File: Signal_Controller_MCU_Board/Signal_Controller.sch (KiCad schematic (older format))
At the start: 50 parts, among them J1 BARREL_JACK, J2 USB_OTG, J3 CONN_02X03, J4 CONN_01X03, J5 CONN_01X02, J6 CONN_01X02, J7 CONN_01X02, J8 CONN_01X07, Q1 2N7002P,215, Q2 2N7002P,215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

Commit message: Both boards mostly completed
just need final tweaks, silkscreen stuff etc, all major routing and
placement done
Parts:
- removed J7: CONN_01X02, symbol CONN_01X02
- added C10: CP1, Capacitors_THT:CP_Radial_D6.3mm_P2.50mm, symbol CP1
- C7, C8: value 18pF -> 22pF
- Y1: footprint (none) -> Crystals:Crystal_SMD_3225-4pin_3.2x2.5mm
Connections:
- net +12V: now also C10.1
- net COIL_1A: now also J5.1 (P1); no longer J5.2 (P2)
- net COIL_1B: now also J5.2 (P2); no longer J5.1 (P1)
- net GND: now also C10.2
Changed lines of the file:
@@
 $EndComp
 $Comp
-L GND #PWR01
+L GND #PWR19
 U 1 1 58F58032
 P 4600 5850
-F 0 "#PWR01" H 4600 5600 50  0001 C CNN
+F 0 "#PWR19" H 4600 5600 50  0001 C CNN
 F 1 "GND" H 4600 5700 50  0000 C CNN
 F 2 "" H 4600 5850 50  0001 C CNN
@@
 $EndComp
 $Comp
-L GND #PWR02
+L GND #PWR1
 U 1 1 58F581C2
 P 950 3550
-F 0 "#PWR02" H 950 3300 50  0001 C CNN
+F 0 "#PWR1" H 950 3300 50  0001 C CNN
 F 1 "GND" H 950 3400 50  0000 C CNN
 F 2 "" H 950 3550 50  0001 C CNN
@@
 $EndComp
 $Comp
-L GND #PWR03
+L GND #PWR9
 U 1 1 58F6B32F
 P 3250 1750
-F 0 "#PWR03" H 3250 1500 50  0001 C CNN
+F 0 "#PWR9" H 3250 1500 50  0001 C CNN
 F 1 "GND" H 3250 1600 50  0000 C CNN
 F 2 "" H 3250 1750 50  0001 C CNN
@@
 $EndComp
 $Comp
-L +5V #PWR04
+L +5V #PWR17
 U 1 1 58F6B398
 P 4300 1050
-F 0 "#PWR04" H 4300 900 50  0001 C CNN
+F 0 "#PWR17" H 4300 900 50  0001 C CNN
 F 1 "+5V" H 4300 1190 50  0000 C CNN
 F 2 "" H 4300 1050 50  0001 C CNN
@@
 $EndComp
 $Comp
-L +12V #PWR05
+L +12V #PWR8
 U 1 1 58F6B3C8
 P 2550 1050
-F 0 "#PWR05" H 2550 900 50  0001 C CNN
+F 0 "#PWR8" H 2550 900 50  0001 C CNN
 F 1 "+12V" H 2550 1190 50  0000 C CNN
 F 2 "" H 2550 1050 50  0001 C CNN
@@
 $EndComp
 $Comp
-L GND #PWR06
+L GND #PWR16
 U 1 1 58F6B932
 P 4150 2100
-F 0 "#PWR06" H 4150 1850 50  0001 C CNN
+F 0 "#PWR16" H 4150 1850 50  0001 C CNN
 F 1 "GND" H 4150 1950 50  0000 C CNN
 F 2 "" H 4150 2100 50  0001 C CNN
@@
 $EndComp
 $Comp
-L +12V #PWR07
+L +12V #PWR4
 U 1 1 58F6BF50
 P 1350 1050
-F 0 "#PWR07" H 1350 900 50  0001 C CNN
+F 0 "#PWR4" H 1350 900 50  0001 C CNN
 F 1 "+12V" H 1350 1190 50  0000 C CNN
 F 2 "" H 1350 1050 50  0001 C CNN
@@
 $EndComp
 $Comp
-L GND #PWR08
+L GND #PWR5
 U 1 1 58F6BFB3
-P 1350 1450
-F 0 "#PWR08" H 1350 1200 50  0001 C CNN
-F 1 "GND" H 1350 1300 50  0000 C CNN
-F 2 "" H 1350 1450 50  0001 C CNN
-F 3 "" H 1350 1450 50  0001 C CNN
-	1    1350 1450
+P 1350 1600
+F 0 "#PWR5" H 1350 1350 50  0001 C CNN
+F 1 "GND" H 1350 1450 50  0000 C CNN
+F 2 "" H 1350 1600 50  0001 C CNN
+F 3 "" H 1350 1600 50  0001 C CNN
+	1    1350 1600
 	1    0    0    -1
 $EndComp
@@
 $EndComp
 $Comp
-L +5V #PWR09
+L +5V #PWR12
 U 1 1 58F6C802
 P 3300 3800
-F 0 "#PWR09" H 3300 3650 50  0001 C CNN
+F 0 "#PWR12" H 3300 3650 50  0001 C CNN
 F 1 "+5V" H 3300 3940 50  0000 C CNN
 F 2 "" H 3300 3800 50  0001 C CNN
@@
 $EndComp
 $Comp
-L GND #PWR010
+L GND #PWR13
 U 1 1 58F6D034
 P 3300 4800
-F 0 "#PWR010" H 3300 4550 50  0001 C CNN
+F 0 "#PWR13" H 3300 4550 50  0001 C CNN
 F 1 "GND" H 3300 4650 50  0000 C CNN
 F 2 "" H 3300 4800 50  0001 C CNN
@@
 $EndComp
 $Comp
-L +5V #PWR011
+L +5V #PWR18
 U 1 1 58F6D787
 P 4600 2750
-F 0 "#PWR011" H 4600 2600 50  0001 C CNN
+F 0 "#PWR18" H 4600 2600 50  0001 C CNN
 F 1 "+5V" H 4600 2890 50  0000 C CNN
 F 2 "" H 4600 2750 50  0001 C CNN
@@
 MOSI
 $Comp
-L +5V #PWR012
+L +5V #PWR21
 U 1 1 58F6E151
 P 6000 1150
-F 0 "#PWR012" H 6000 1000 50  0001 C CNN
+F 0 "#PWR21" H 6000 1000 50  0001 C CNN
 F 1 "+5V" H 6000 1290 50  0000 C CNN
 F 2 "" H 6000 1150 50  0001 C CNN
@@
 $EndComp
 $Comp
-L GND #PWR013
+L GND #PWR22
 U 1 1 58F6E17B
 P 6000 1550
-F 0 "#PWR013" H 6000 1300 50  0001 C CNN
+F 0 "#PWR22" H 6000 1300 50  0001 C CNN
 F 1 "GND" H 6000 1400 50  0000 C CNN
 F 2 "" H 6000 1550 50  0001 C CNN
@@
 $EndComp
 $Comp
-L GND #PWR014
+L GND #PWR7
 U 1 1 58F6F39D
 P 1950 3650
-F 0 "#PWR014" H 1950 3400 50  0001 C CNN
+F 0 "#PWR7" H 1950 3400 50  0001 C CNN
 F 1 "GND" H 1950 3500 50  0000 C CNN
 F 2 "" H 1950 3650 50  0001 C CNN
@@
 F 0 "Y1" H 4100 5050 50  0000 C CNN
 F 1 "Crystal" V 3950 5050 50  0000 C CNN
-F 2 "" H 4100 4900 50  0001 C CNN
+F 2 "Crystals:Crystal_SMD_3225-4pin_3.2x2.5mm" H 4100 4900 50  0001 C CNN
 F 3 "" H 4100 4900 50  0001 C CNN
 	1    4100 4900
@@
 P 3850 4700
 F 0 "C7" V 3800 4550 50  0000 L CNN
-F 1 "18pF" V 3900 4450 50  0000 L CNN
+F 1 "22pF" V 3900 4450 50  0000 L CNN
 F 2 "Capacitors_SMD:C_0603" H 3888 4550 50  0001 C CNN
 F 3 "" H 3850 4700 50  0001 C CNN
@@
 P 3850 5100
 F 0 "C8" V 3900 4950 50  0000 L CNN
-F 1 "18pF" V 3800 4850 50  0000 L CNN
+F 1 "22pF" V 3800 4850 50  0000 L CNN
 F 2 "Capacitors_SMD:C_0603" H 3888 4950 50  0001 C CNN
 F 3 "" H 3850 5100 50  0001 C CNN
@@
 $EndComp
 $Comp
-L GND #PWR015
+L GND #PWR14
 U 1 1 58F6FF32
 P 3650 5300
-F 0 "#PWR015" H 3650 5050 50  0001 C CNN
+F 0 "#PWR14" H 3650 5050 50  0001 C CNN
 F 1 "GND" H 3650 5150 50  0000 C CNN
 F 2 "" H 3650 5300 50  0001 C CNN
@@
 $EndComp
 $Comp
-L GND #PWR016
+L GND #PWR25
 U 1 1 58F716B0
 P 8000 5850
-F 0 "#PWR016" H 8000 5600 50  0001 C CNN
+F 0 "#PWR25" H 8000 5600 50  0001 C CNN
 F 1 "GND" H 8000 5700 50  0000 C CNN
 F 2 "" H 8000 5850 50  0001 C CNN
@@
 $EndComp
 $Comp
-L GND #PWR017
+L GND #PWR15
 U 1 1 58F71A74
 P 3900 3350
-F 0 "#PWR017" H 3900 3100 50  0001 C CNN
+F 0 "#PWR15" H 3900 3100 50  0001 C CNN
 F 1 "GND" H 3900 3200 50  0000 C CNN
 F 2 "" H 3900 3350 50  0001 C CNN
@@
 $EndComp
 $Comp
-L +5V #PWR018
+L +5V #PWR10
 U 1 1 58F73DF5
 P 3300 2750
-F 0 "#PWR018" H 3300 2600 50  0001 C CNN
+F 0 "#PWR10" H 3300 2600 50  0001 C CNN
 F 1 "+5V" H 3300 2890 50  0000 C CNN
 F 2 "" H 3300 2750 50  0001 C CNN
@@
 $EndComp
 $Comp
-L GND #PWR019
+L GND #PWR11
 U 1 1 58F73E45
 P 3300 3350
-F 0 "#PWR019" H 3300 3100 50  0001 C CNN
+F 0 "#PWR11" H 3300 3100 50  0001 C CNN
 F 1 "GND" H 3300 3200 50  0000 C CNN
 F 2 "" H 3300 3350 50  0001 C CNN
@@
 $EndComp
 $Comp
-L +12V #PWR020
+L +12V #PWR26
 U 1 1 58F75C3C
 P 9050 1100
-F 0 "#PWR020" H 9050 950 50  0001 C CNN
+F 0 "#PWR26" H 9050 950 50  0001 C CNN
 F 1 "+12V" H 9050 1240 50  0000 C CNN
 F 2 "" H 9050 1100 50  0001 C CNN
@@
 $EndComp
 $Comp
-L +12V #PWR021
+L +12V #PWR27
 U 1 1 58F76B58
 P 9050 3050
-F 0 "#PWR021" H 9050 2900 50  0001 C CNN
+F 0 "#PWR27" H 9050 2900 50  0001 C CNN
 F 1 "+12V" H 9050 3190 50  0000 C CNN
 F 2 "" H 9050 3050 50  0001 C CNN
@@
 $EndComp
 $Comp
-L +12V #PWR022
+L +12V #PWR28
 U 1 1 58F77023
 P 9050 4900
-F 0 "#PWR022" H 9050 4750 50  0001 C CNN
+F 0 "#PWR28" H 9050 4750 50  0001 C CNN
 F 1 "+12V" H 9050 5040 50  0000 C CNN
 F 2 "" H 9050 4900 50  0001 C CNN
@@
 $EndComp
 $Comp
-L GND #PWR023
+L GND #PWR29
 U 1 1 58F77940
 P 9250 2550
-F 0 "#PWR023" H 9250 2300 50  0001 C CNN
+F 0 "#PWR29" H 9250 2300 50  0001 C CNN
 F 1 "GND" H 9250 2400 50  0000 C CNN
 F 2 "" H 9250 2550 50  0001 C CNN
@@
 $EndComp
 $Comp
-L GND #PWR024
+L GND #PWR30
 U 1 1 58F77BFD
 P 9250 4450
-F 0 "#PWR024" H 9250 4200 50  0001 C CNN
+F 0 "#PWR30" H 9250 4200 50  0001 C CNN
 F 1 "GND" H 9250 4300 50  0000 C CNN
 F 2 "" H 9250 4450 50  0001 C CNN
@@
 $EndComp
 $Comp
-L GND #PWR025
+L GND #PWR31
 U 1 1 58F782F4
 P 9250 6300
-F 0 "#PWR025" H 9250 6050 50  0001 C CNN
+F 0 "#PWR31" H 9250 6050 50  0001 C CNN
 F 1 "GND" H 9250 6150 50  0000 C CNN
 F 2 "" H 9250 6300 50  0001 C CNN
@@
 Relay Expansion Board
 $Comp
-L GND #PWR026
+L GND #PWR24
 U 1 1 58F7EA21
 P 7600 1650
-F 0 "#PWR026" H 7600 1400 50  0001 C CNN
+F 0 "#PWR24" H 7600 1400 50  0001 C CNN
 F 1 "GND" H 7600 1500 50  0000 C CNN
 F 2 "" H 7600 1650 50  0001 C CNN
@@
 $EndComp
 $Comp
-L +12V #PWR027
+L +12V #PWR23
 U 1 1 58F7EBD9
 P 7600 1050
-F 0 "#PWR027" H 7600 900 50  0001 C CNN
+F 0 "#PWR23" H 7600 900 50  0001 C CNN
 F 1 "+12V" H 7600 1190 50  0000 C CNN
 F 2 "" H 7600 1050 50  0001 C CNN
@@
 $EndComp
 $Comp
-L GND #PWR028
+L GND #PWR3
 U 1 1 58F838E9
 P 1250 7400
-F 0 "#PWR028" H 1250 7150 50  0001 C CNN
+F 0 "#PWR3" H 1250 7150 50  0001 C CNN
 F 1 "GND" H 1250 7250 50  0000 C CNN
 F 2 "" H 1250 7400 50  0001 C CNN
@@
 BUTTON_4
 $Comp
-L +5V #PWR029
+L +5V #PWR2
 U 1 1 58F842B6
 P 1250 6400
-F 0 "#PWR029" H 1250 6250 50  0001 C CNN
+F 0 "#PWR2" H 1250 6250 50  0001 C CNN
 F 1 "+5V" H 1250 6540 50  0000 C CNN
 F 2 "" H 1250 6400 50  0001 C CNN
@@
 Text Notes 2000 6200 0    60   ~ 0
 Control Buttons\n
-$Comp
-L CONN_01X02 J7
-U 1 1 58F84517
-P 1650 1200
-F 0 "J7" H 1650 1350 50  0000 C CNN
-F 1 "CONN_01X02" V 1750 1200 50  0000 C CNN
-F 2 "" H 1650 1200 50  0001 C CNN
-F 3 "" H 1650 1200 50  0001 C CNN
-	1    1650 1200
-	1    0    0    -1
-$EndComp
 $Comp
 L CONN_01X02 J5
@@
 Text Notes 650  850  0    60   ~ 0
 Barrel or Terminal Block
+Text HLabel 1400 4750 2    60   Input ~ 0
+COIL_1A
 Text HLabel 1400 4650 2    60   Input ~ 0
-COIL_1A
-Text HLabel 1400 4750 2    60   Input ~ 0
 COIL_1B
 Text HLabel 1400 5150 2    60   Input ~ 0
 BULB_1
 $Comp
-L GND #PWR030
+L GND #PWR6
 U 1 1 58F8727C
 P 1400 5350
-F 0 "#PWR030" H 1400 5100 50  0001 C CNN
+F 0 "#PWR6" H 1400 5100 50  0001 C CNN
 F 1 "GND" H 1400 5200 50  0000 C CNN
 F 2 "" H 1400 5350 50  0001 C CNN
@@
 GPIO_6
 $Comp
-L GND #PWR031
+L GND #PWR20
 U 1 1 58FA74E4
 P 5950 7150
-F 0 "#PWR031" H 5950 6900 50  0001 C CNN
+F 0 "#PWR20" H 5950 6900 50  0001 C CNN
 F 1 "GND" H 5950 7000 50  0000 C CNN
 F 2 "" H 5950 7150 50  0001 C CNN
@@
 	1    0    0    -1
 $EndComp
+$Comp
+L CP1 C10
+U 1 1 58FAE842
+P 1550 1350
+F 0 "C10" H 1575 1450 50  0000 L CNN
+F 1 "CP1" H 1575 1250 50  0000 L CNN
+F 2 "Capacitors_THT:CP_Radial_D6.3mm_P2.50mm" H 1550 1350 50  0001 C CNN
+F 3 "" H 1550 1350 50  0001 C CNN
+	1    1550 1350
+	1    0    0    -1
+$EndComp
 Wire Wire Line
 	4600 5750 4700 5750
@@
 	1250 1350 1350 1350
 Wire Wire Line
-	1350 1250 1350 1450
-Wire Wire Line
-	1250 1250 1450 1250
+	1350 1250 1350 1600
 Connection ~ 1350 1350
-Wire Wire Line
-	1250 1150 1450 1150
 Wire Wire Line
 	1350 1150 1350 1050
@@
 	2700 6500 2700 6450
 Connection ~ 2700 6450
-Connection ~ 1350 1150
-Connection ~ 1350 1250
 Wire Wire Line
 	1300 5250 1400 5250
@@
 	1950 2850 1950 2800
 Connection ~ 1950 2800
+Wire Wire Line
+	1250 1150 1550 1150
+Wire Wire Line
+	1350 1250 1250 1250
+Wire Wire Line
+	1550 1150 1550 1200
+Connection ~ 1350 1150
+Wire Wire Line
+	1550 1500 1550 1550
+Wire Wire Line
+	1550 1550 1350 1550
+Connection ~ 1350 1550
 $EndSCHEMATC

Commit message: I looked at it (minor tweaks)
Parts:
- C1: value 10uF -> 1uF
- C9: value 0.1uF -> 1uF
- R1, R3, R6: value R -> 1K
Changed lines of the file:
@@
 P 4150 1450
 F 0 "R3" V 4230 1450 50  0000 C CNN
-F 1 "R" V 4150 1450 50  0000 C CNN
+F 1 "1K" V 4150 1450 50  0000 C CNN
 F 2 "Resistors_SMD:R_0603" V 4080 1450 50  0001 C CNN
 F 3 "" H 4150 1450 50  0001 C CNN
@@
 P 1950 3000
 F 0 "R1" V 2030 3000 50  0000 C CNN
-F 1 "R" V 1950 3000 50  0000 C CNN
+F 1 "1K" V 1950 3000 50  0000 C CNN
 F 2 "Resistors_SMD:R_0603" V 1880 3000 50  0001 C CNN
 F 3 "" H 1950 3000 50  0001 C CNN
@@
 P 2150 3000
 F 0 "C1" H 2175 3100 50  0000 L CNN
-F 1 "10uF" H 2175 2900 50  0000 L CNN
+F 1 "1uF" H 2175 2900 50  0000 L CNN
 F 2 "Capacitors_SMD:C_0603" H 2188 2850 50  0001 C CNN
 F 3 "" H 2150 3000 50  0001 C CNN
@@
 P 4200 3250
 F 0 "C9" V 4250 3300 50  0000 L CNN
-F 1 "0.1uF" V 4150 3000 50  0000 L CNN
+F 1 "1uF" V 4150 3000 50  0000 L CNN
 F 2 "Capacitors_SMD:C_0603" H 4238 3100 50  0001 C CNN
 F 3 "" H 4200 3250 50  0001 C CNN
@@
 P 8200 5150
 F 0 "R6" V 8280 5150 50  0000 C CNN
-F 1 "R" V 8200 5150 50  0000 C CNN
+F 1 "1K" V 8200 5150 50  0000 C CNN
 F 2 "Resistors_SMD:R_0603" V 8130 5150 50  0001 C CNN
 F 3 "" H 8200 5150 50  0001 C CNN

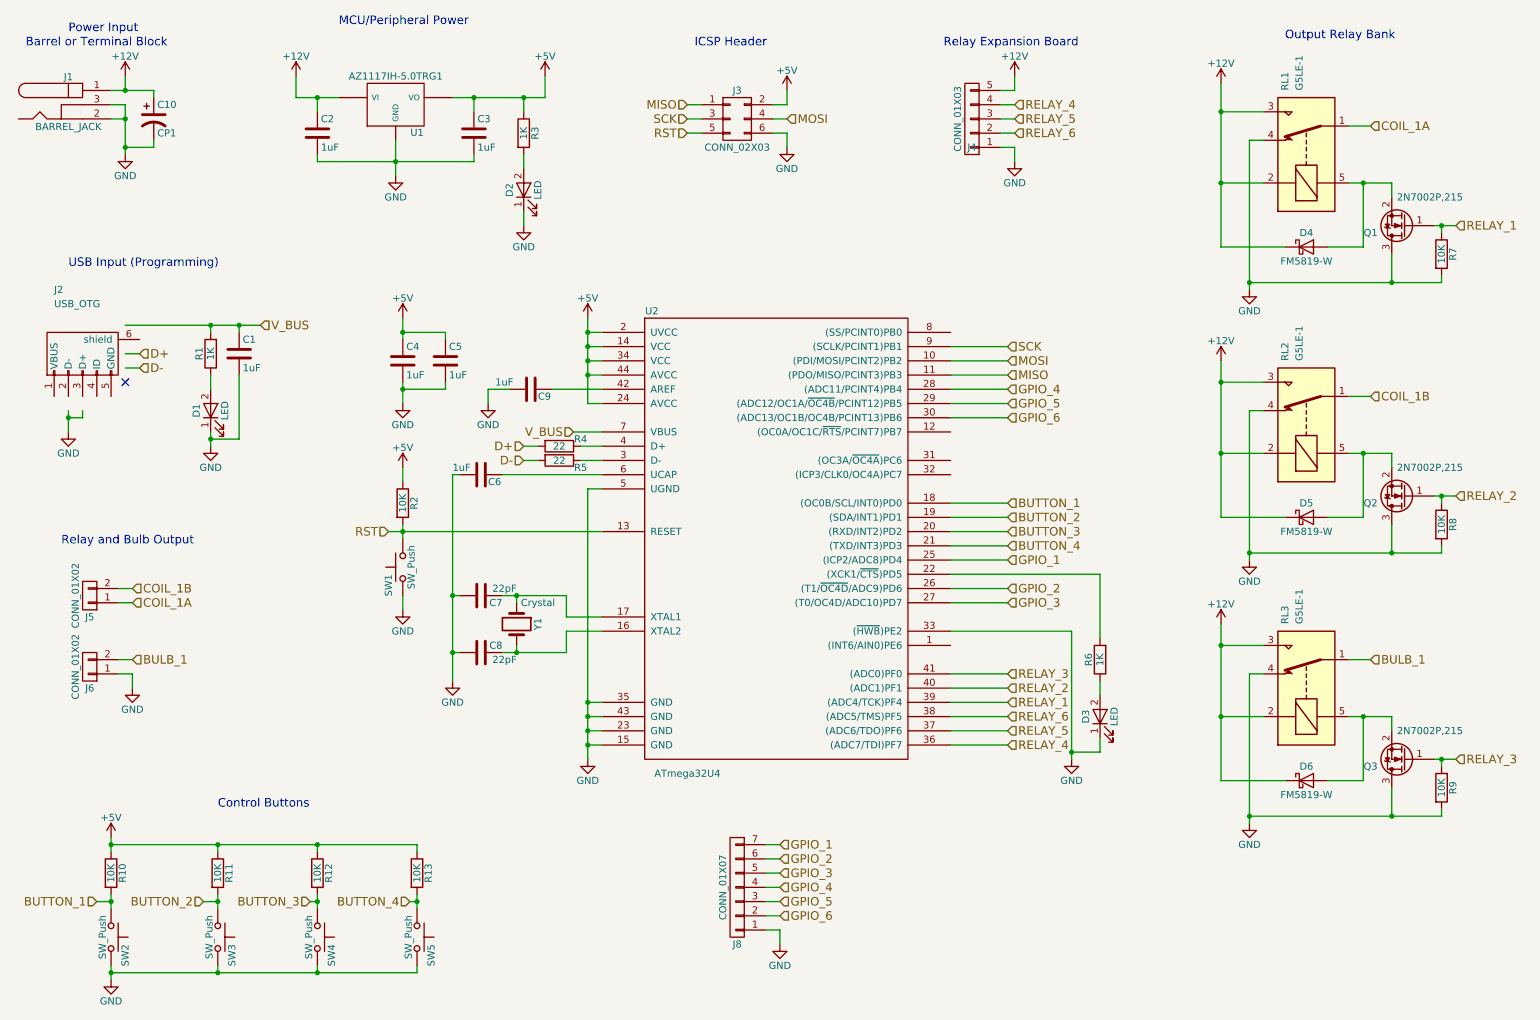
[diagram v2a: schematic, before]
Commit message: breaking out a UART instead of just 6 GPIO
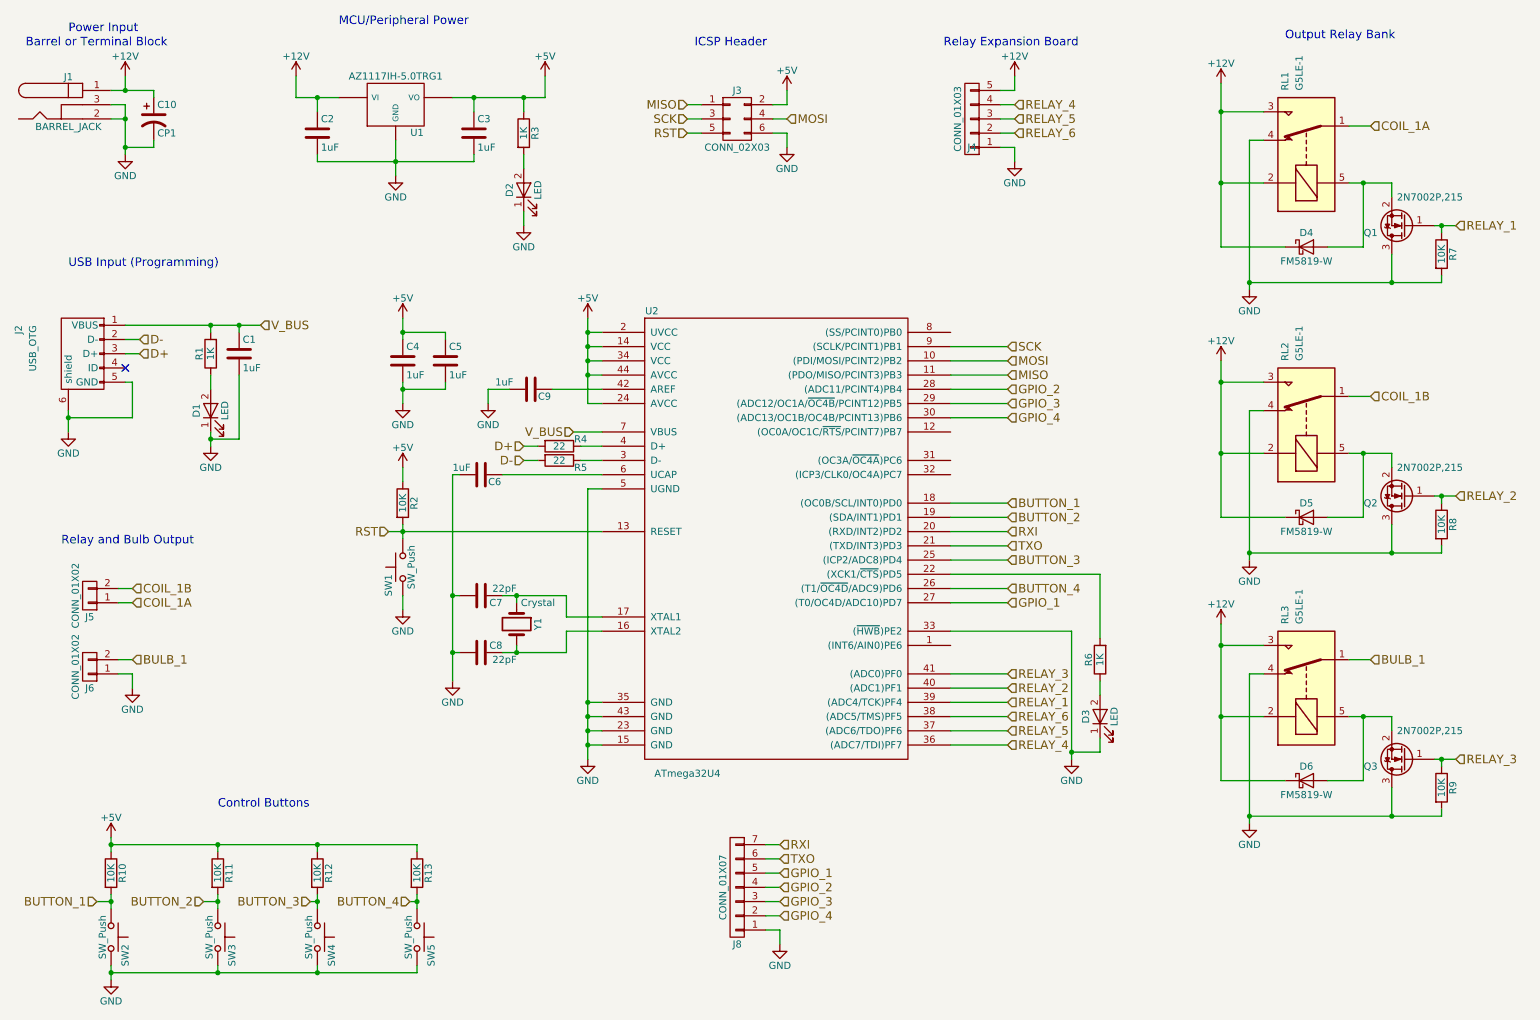
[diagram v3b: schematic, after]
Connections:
- net GPIO_5 is gone; now on net GPIO_3: J8.3 (P3), U2.29 ((ADC12/OC1A/~OC4B~/PCINT12)PB5)
- net GPIO_6 is gone; now on net GPIO_4: J8.2 (P2), U2.30 ((ADC13/OC1B/OC4B/PCINT13)PB6)
- net BUTTON_3: now also U2.25 ((ICP2/ADC8)PD4); no longer U2.20 ((RXD/INT2)PD2)
- net BUTTON_4: now also U2.26 ((T1/~OC4D~/ADC9)PD6); no longer U2.21 ((TXD/INT3)PD3)
- net D+: now also J2.3 (D+)
- net D-: now also J2.2 (D-)
- net GND: now also J2.5 (GND), J2.6 (shield)
- net GPIO_1: now also J8.5 (P5), U2.27 ((T0/OC4D/ADC10)PD7); no longer J8.7 (P7), U2.25 ((ICP2/ADC8)PD4)
- net GPIO_2: now also J8.4 (P4), U2.28 ((ADC11/PCINT4)PB4); no longer J8.6 (P6), U2.26 ((T1/~OC4D~/ADC9)PD6)
- net GPIO_3: no longer J8.5 (P5), U2.27 ((T0/OC4D/ADC10)PD7)
- net GPIO_4: no longer J8.4 (P4), U2.28 ((ADC11/PCINT4)PB4)
- net V_BUS: now also J2.1 (VBUS)
- new net RXI: J8.7 (P7), U2.20 ((RXD/INT2)PD2)
- new net TXO: J8.6 (P6), U2.21 ((TXD/INT3)PD3)
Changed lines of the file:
@@
 LIBS:switches
 LIBS:relays
-LIBS:Global_Parts
 LIBS:Signal_Controller-cache
 EELAYER 25 0
@@
 F 3 "" H 1200 2950 50  0001 C CNN
 	1    1050 3000
-	1    0    0    -1
+	0    -1   1    0
 $EndComp
 $Comp
@@
 Text HLabel 1450 3000 2    60   Input ~ 0
 D+
-Text HLabel 1450 3100 2    60   Input ~ 0
+Text HLabel 1450 2900 2    60   Input ~ 0
 D-
-NoConn ~ 1350 3200
+NoConn ~ 1350 3100
 $Comp
 L R R1
@@
 	0    -1   -1   0
 $EndComp
-Text HLabel 7550 4450 2    60   Input ~ 0
+Text HLabel 7550 4250 2    60   Input ~ 0
+RXI
+Text HLabel 7550 4350 2    60   Input ~ 0
+TXO
+Text HLabel 7550 4750 2    60   Input ~ 0
 GPIO_1
-Text HLabel 7550 4650 2    60   Input ~ 0
+Text HLabel 7550 3250 2    60   Input ~ 0
 GPIO_2
-Text HLabel 7550 4750 2    60   Input ~ 0
-GPIO_3
-Text HLabel 7550 3250 2    60   Input ~ 0
-GPIO_4
 Text HLabel 7550 4050 2    60   Input ~ 0
 BUTTON_1
 Text HLabel 7550 3350 2    60   Input ~ 0
-GPIO_5
+GPIO_3
 Text HLabel 7550 3450 2    60   Input ~ 0
-GPIO_6
+GPIO_4
 Text HLabel 7550 4150 2    60   Input ~ 0
 BUTTON_2
-Text HLabel 7550 4250 2    60   Input ~ 0
+Text HLabel 7550 4450 2    60   Input ~ 0
 BUTTON_3
-Text HLabel 7550 4350 2    60   Input ~ 0
+Text HLabel 7550 4650 2    60   Input ~ 0
 BUTTON_4
 $Comp
@@
 $EndComp
 Text HLabel 5950 6450 2    60   Input ~ 0
+RXI
+Text HLabel 5950 6550 2    60   Input ~ 0
+TXO
+Text HLabel 5950 6650 2    60   Input ~ 0
 GPIO_1
-Text HLabel 5950 6550 2    60   Input ~ 0
+Text HLabel 5950 6750 2    60   Input ~ 0
 GPIO_2
-Text HLabel 5950 6650 2    60   Input ~ 0
+Text HLabel 5950 6850 2    60   Input ~ 0
 GPIO_3
-Text HLabel 5950 6750 2    60   Input ~ 0
+Text HLabel 5950 6950 2    60   Input ~ 0
 GPIO_4
-Text HLabel 5950 6850 2    60   Input ~ 0
-GPIO_5
-Text HLabel 5950 6950 2    60   Input ~ 0
-GPIO_6
 $Comp
 L GND #PWR20
@@
 Wire Wire Line
 	950  3400 950  3550
-Wire Wire Line
-	950  3450 1050 3450
-Wire Wire Line
-	1050 3450 1050 3400
 Connection ~ 950  3450
 Wire Wire Line
@@
 	1450 3000 1350 3000
 Wire Wire Line
-	1350 3100 1450 3100
+	1350 2900 1450 2900
 Wire Wire Line
 	1950 3550 1950 3650
@@
 	7150 4750 7550 4750
 Wire Wire Line
-	7550 4650 7150 4650
-Wire Wire Line
-	7150 4450 7550 4450
+	7550 4350 7150 4350
+Wire Wire Line
+	7150 4250 7550 4250
 Wire Wire Line
 	7550 3350 7150 3350
@@
 	7150 4150 7550 4150
 Wire Wire Line
-	7550 4250 7150 4250
-Wire Wire Line
-	7150 4350 7550 4350
+	7550 4450 7150 4450
+Wire Wire Line
+	7150 4650 7550 4650
 Wire Wire Line
 	1150 6850 1250 6850
@@
 	1550 1550 1350 1550
 Connection ~ 1350 1550
+Wire Wire Line
+	950  3450 1400 3450
+Wire Wire Line
+	1400 3450 1400 3200
+Wire Wire Line
+	1400 3200 1350 3200
 $EndSCHEMATC
